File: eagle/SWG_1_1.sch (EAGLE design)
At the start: 20 parts, among them IC1 74HC14N, X1 Out

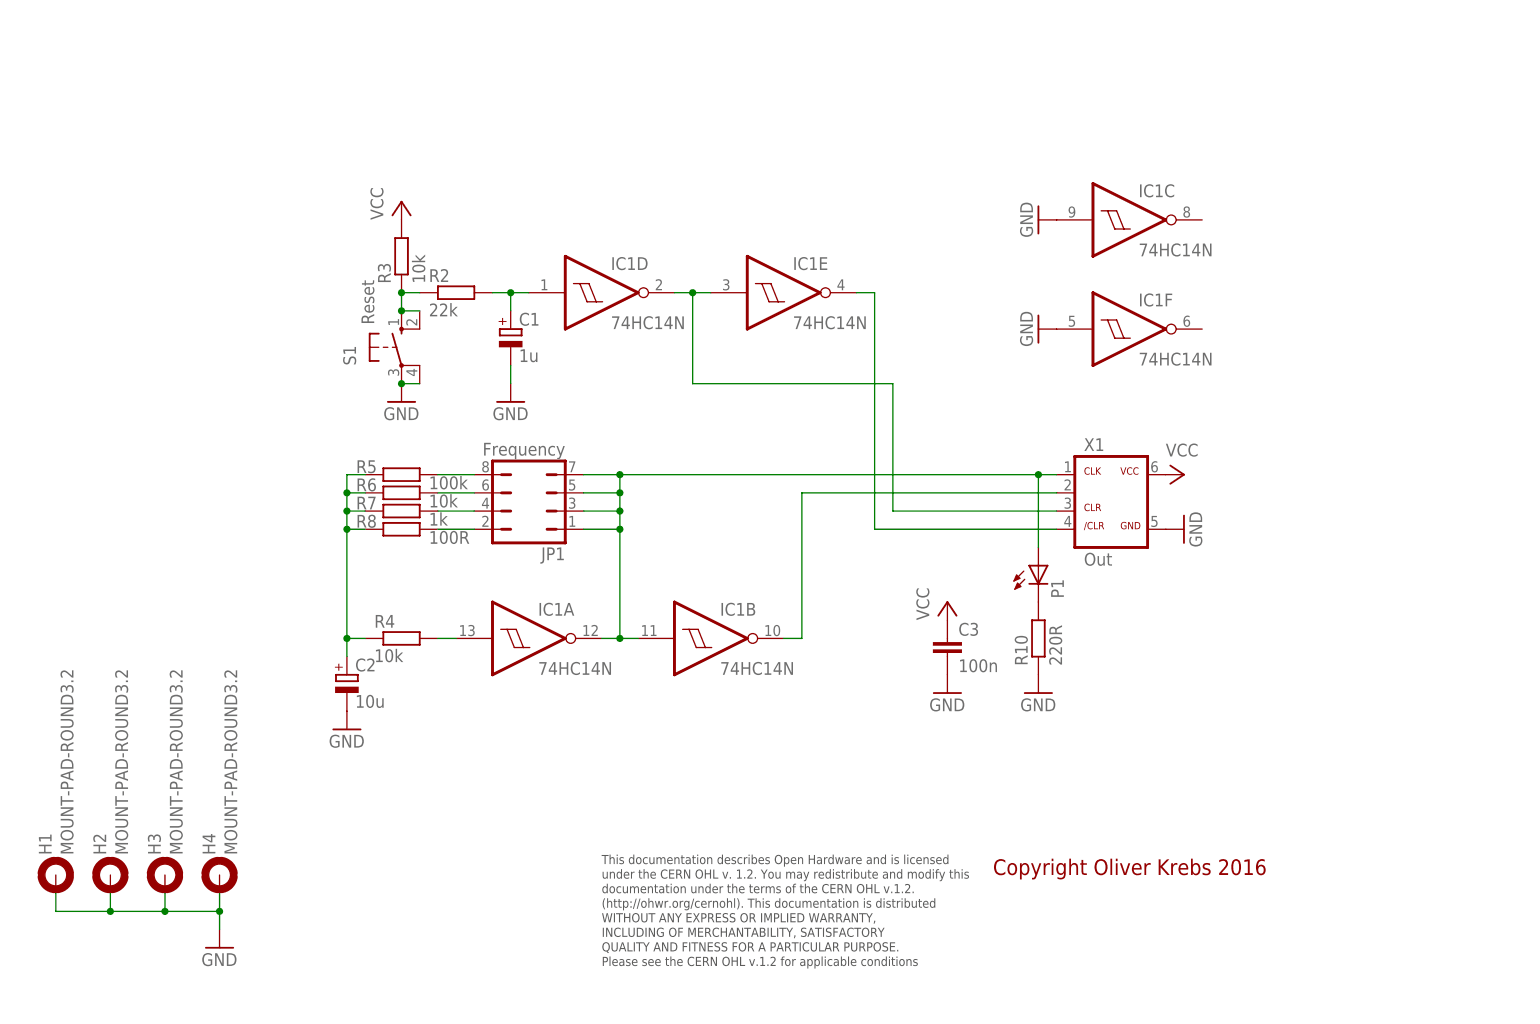
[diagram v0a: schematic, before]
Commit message: Add new tetra-Board and arduino files
Add AMP_1_0, AVC_1_0, D18_1_1, IOP_1_2, MIC_1_0, PIN_1_1, POT_1_0, PWA_1_0, PWR_1_0, RGF 2.0, SOC_2_0, VLT_1_0
Add mex_nano_shield_keyboard, mex_nano_shied_numbers

New arduino projects
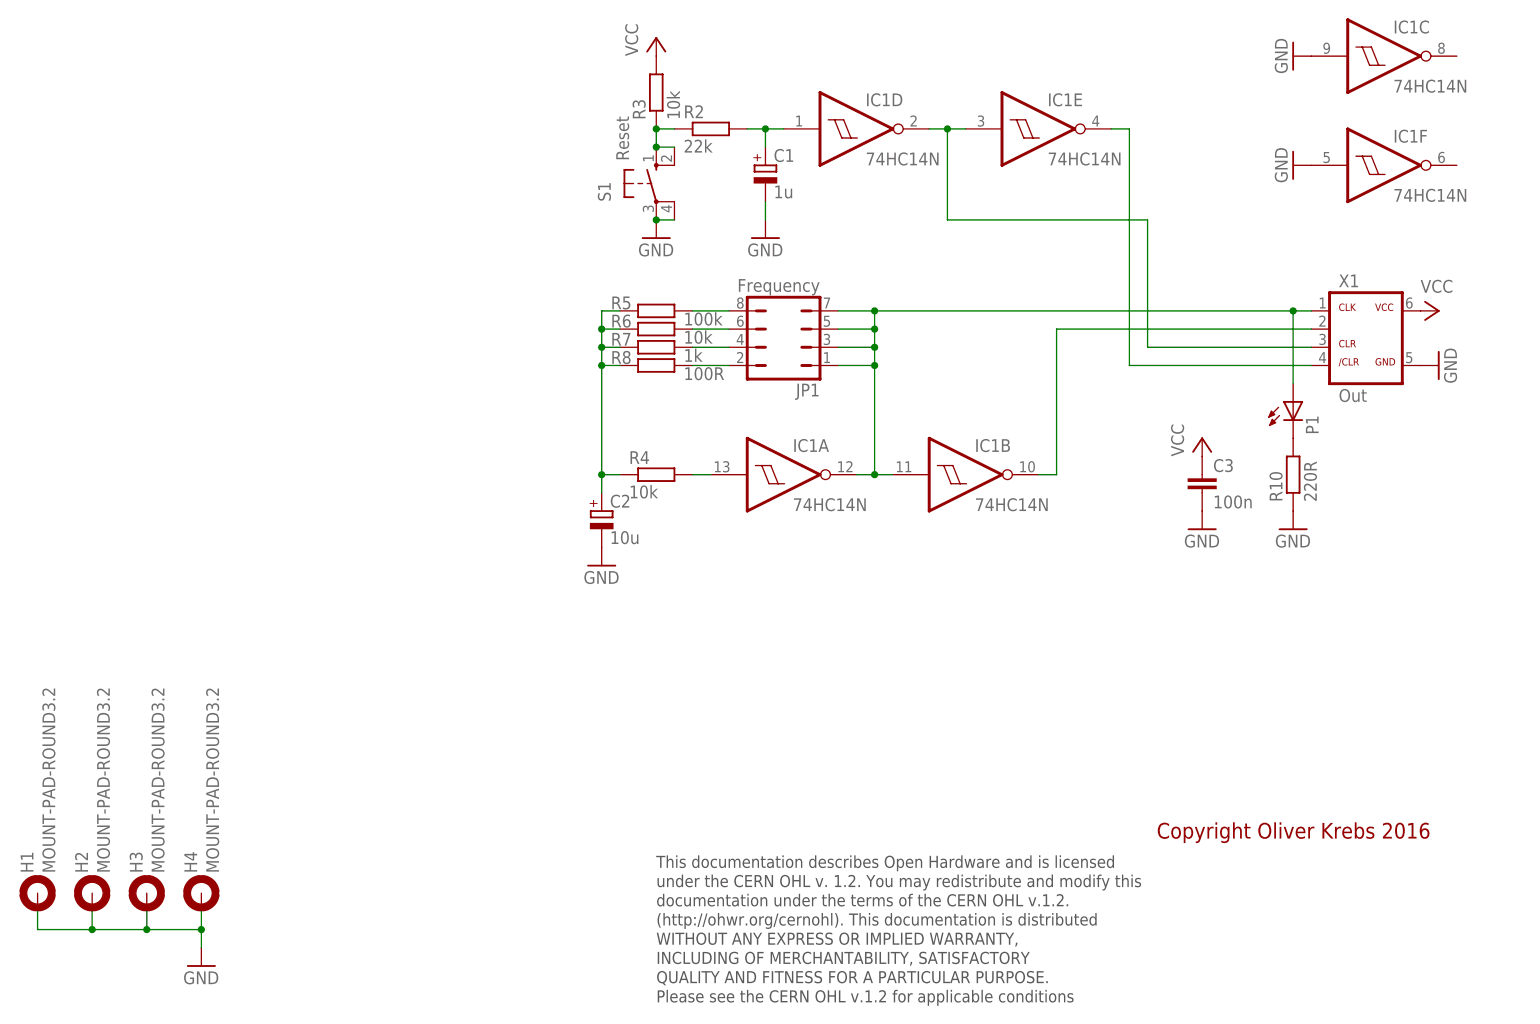
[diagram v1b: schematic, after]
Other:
- moved on the sheet: C1, C2, C3, H1, H2, H3, H4, IC1A, IC1B, IC1C, IC1D, IC1E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
